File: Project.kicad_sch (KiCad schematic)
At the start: 60 parts, among them J1 Power terminal, J3 LED_pins, Q1 BC857, Q2 BC857, Q3 BC857, Q4 BC857, Q5 BC857, Q6 BC857, Q7 BC857, Q8 BC857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

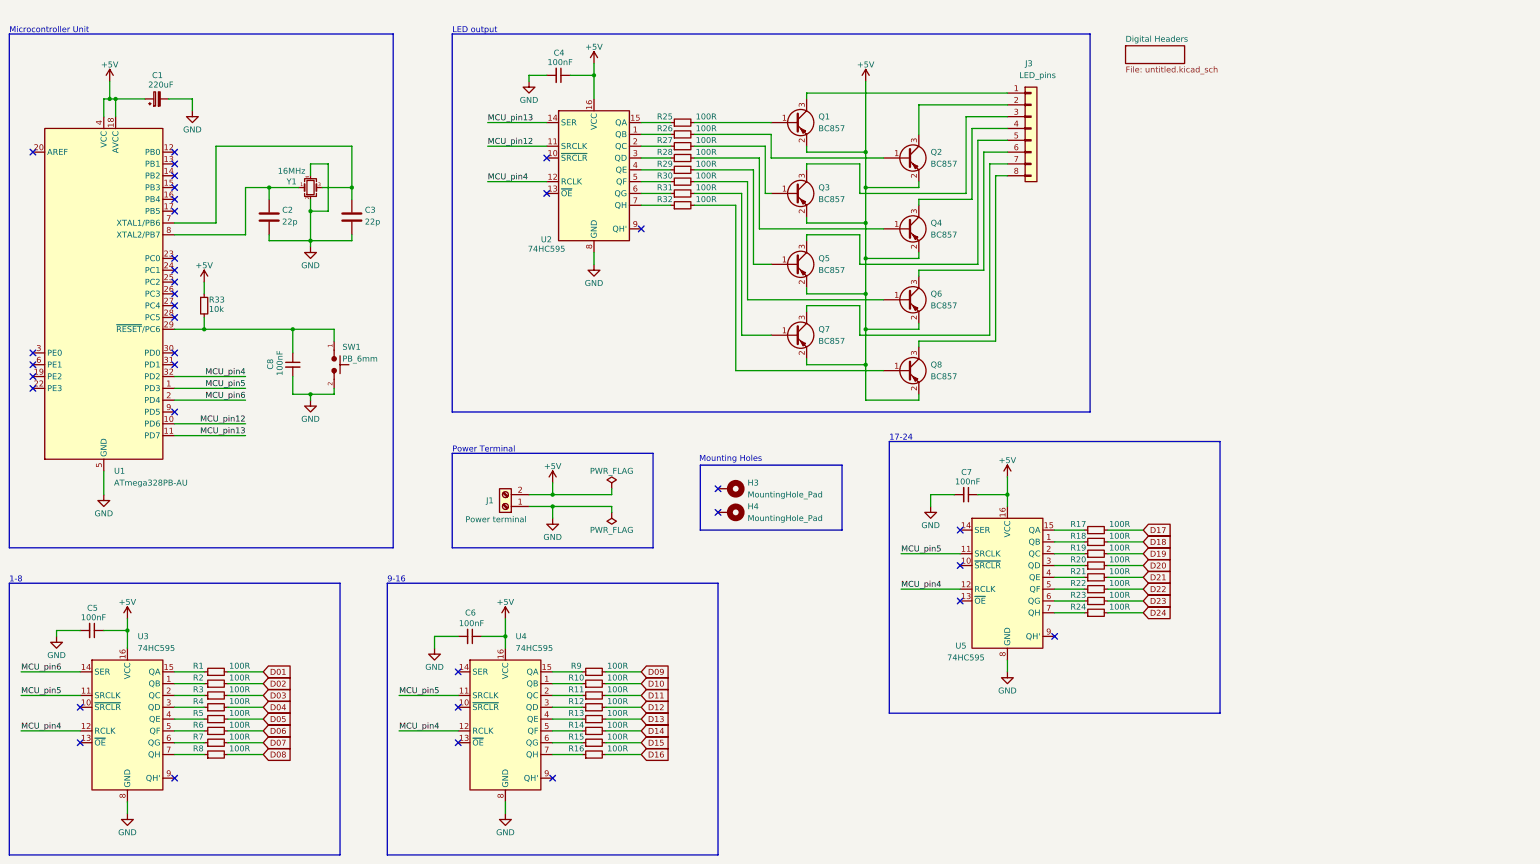
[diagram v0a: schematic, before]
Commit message: PCB design done, BOM still undecided
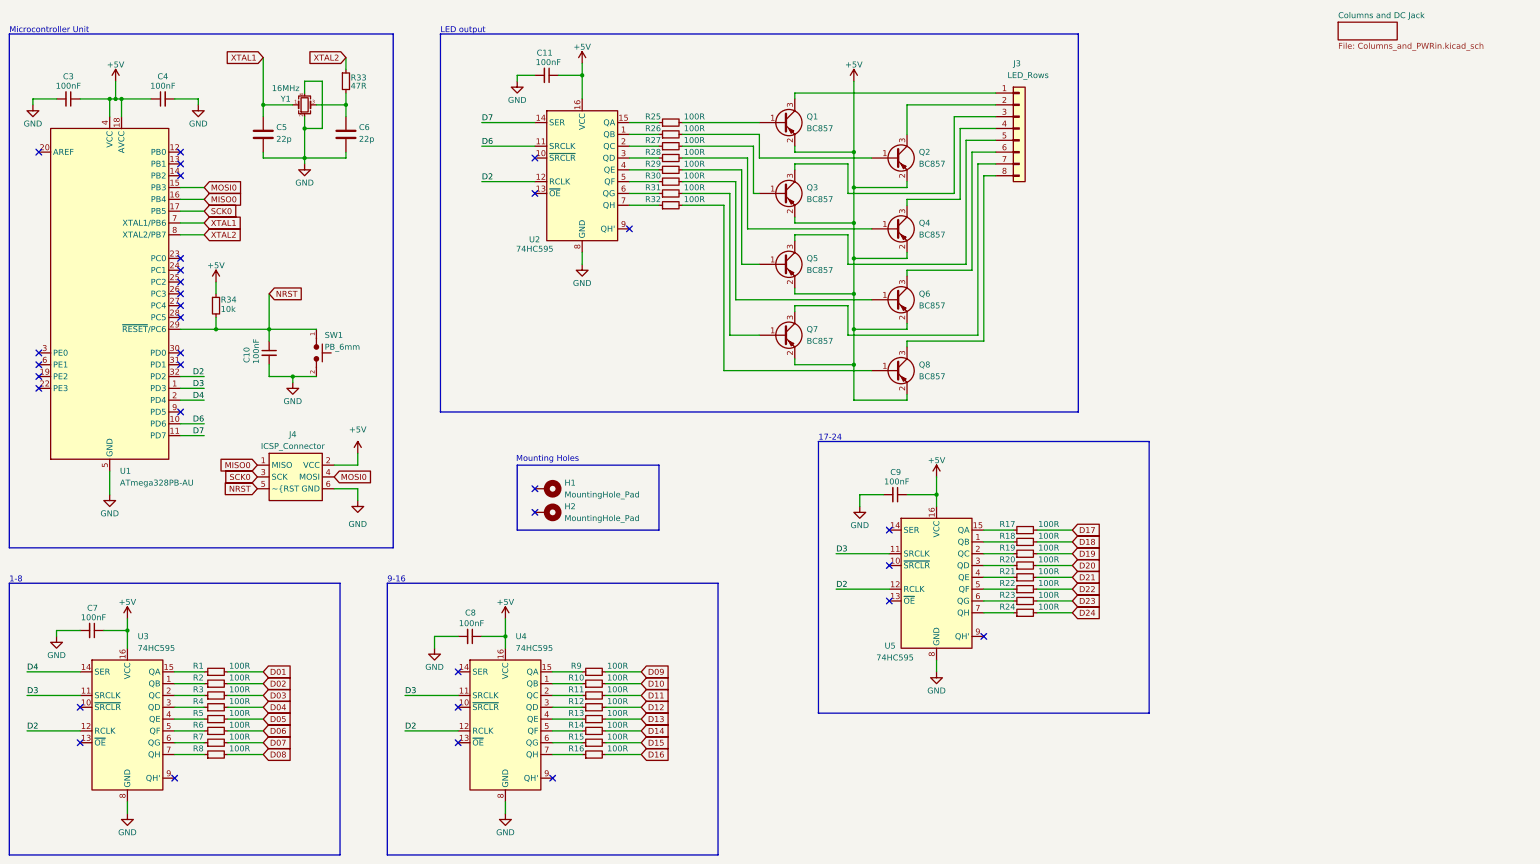
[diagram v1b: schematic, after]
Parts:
- removed C1: 220uF, Capacitor_SMD:CP_Elec_10x10, symbol Device:C_Polarized_Small
- removed C2, C3: 22p, Capacitor_SMD:C_0402_1005Metric, symbol Device:C
- removed H3, H4: MountingHole_Pad, MountingHole:MountingHole_3.2mm_M3_Pad_Via, symbol Mechanical:MountingHole_Pad
- removed J1: Power terminal, TerminalBlock_Phoenix:TerminalBlock_Phoenix_MKDS-1,5-2-5.08_1x02_P5.08mm_Horizontal, symbol Connector:Screw_Terminal_01x02
- added C3, C4: 100nF, Capacitor_SMD:C_0603_1608Metric, symbol Device:C_Small
- added C5, C6: 22p, Capacitor_SMD:C_0402_1005Metric, symbol Device:C
- added H1, H2: MountingHole_Pad, MountingHole:MountingHole_3.2mm_M3_Pad_Via, symbol Mechanical:MountingHole_Pad
- added J4: ICSP_Connector, Connector_PinHeader_2.54mm:PinHeader_2x03_P2.54mm_Vertical, symbol PCM_SL_Connectors:ICSP_Connector
- added R33: 47R, Resistor_SMD:R_0603_1608Metric, symbol Device:R_Small
- J3: value LED_pins -> LED_Rows
- renumbered C8 to C10, C4 to C11, C5 to C7, C6 to C8, C7 to C9, R33 to R34
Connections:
- net +5V: now also C3.1, C4.1, J4.2 (VCC)
- net GND: now also C3.2, C4.2, C5.2, C6.2, J4.6 (GND)
- net XTAL1: now reaches Y1.1
- net XTAL1: now also U1.7 (XTAL1/PB6), C5.1; no longer U1.8 (XTAL2/PB7)
- net at Y1.3: now also C6.1, R33.2; no longer U1.7 (XTAL1/PB6)
- net NRST: now reaches C10.1, R34.2, SW1.1, U1.29 (~{RESET}/PC6)
- net NRST: now also J4.5 (~{RST)
- net MOSI0: now reaches U1.15 (PB3)
- net MOSI0: now also J4.4 (MOSI)
- net MISO0: now reaches U1.16 (PB4)
- net MISO0: now also J4.1 (MISO)
- net SCK0: now reaches U1.17 (PB5)
- net SCK0: now also J4.3 (SCK)
- net MCU_pin12 renamed D6
- net MCU_pin13 renamed D7
- net MCU_pin4 renamed D2
- net MCU_pin5 renamed D3
- net MCU_pin6 renamed D4
- new net XTAL2: R33.1, U1.8 (XTAL2/PB7)
- no-connect marks 36 -> 33
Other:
- sheet Digital Headers renamed Columns and DC Jack
- sheet Columns and DC Jack: file untitled.kicad_sch -> Columns_and_PWRin.kicad_sch
- note removed: "Power Terminal"
- title: LED Array/ Digital Shifting with Atmega328 -> LED Array with Atmega328PB
- moved on the sheet: C10, C11, C9, J3, Q1, Q2, Q3, Q4, Q5, Q6, Q7, Q8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

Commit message: 595 column chip not daisy chained and  floating OE pins mistakes corrected
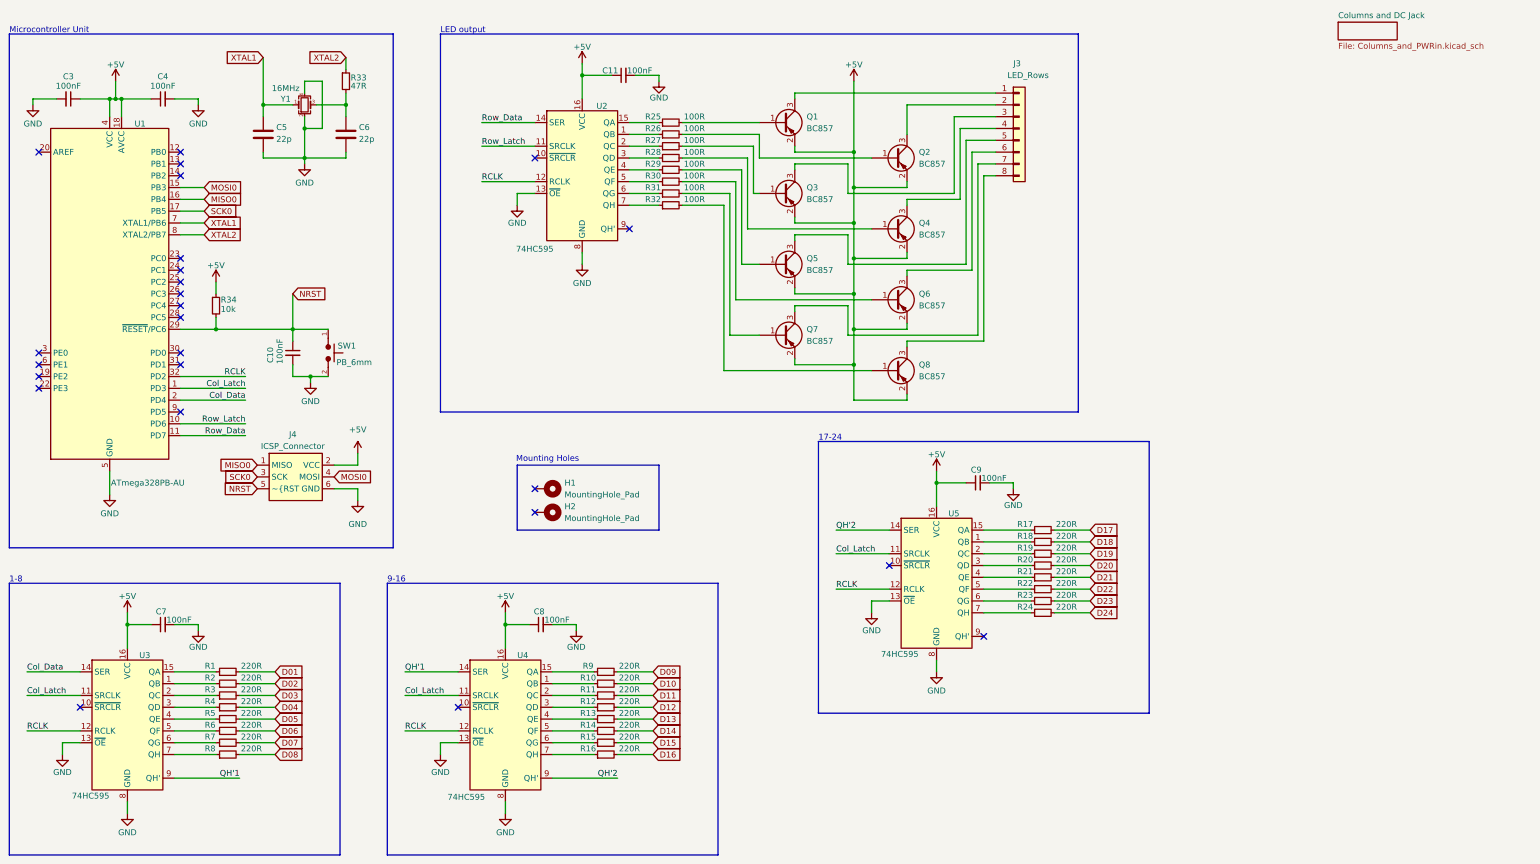
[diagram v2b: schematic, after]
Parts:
- R1, R10, R11, R12, R13, R14, R15, R16, R17, R18, R19, R2, R20, R21, R22, R23, R24, R3, R4, R5, R6, R7, R8, R9: value 100R -> 220R
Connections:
- net GND: now also U2.13 (~{OE}), U3.13 (~{OE}), U4.13 (~{OE}), U5.13 (~{OE})
- net QH'1: now reaches U4.14 (SER)
- net QH'1: now also U3.9 (QH')
- net QH'2: now reaches U4.9 (QH')
- net QH'2: now also U5.14 (SER)
- net D2 renamed RCLK
- net D3 renamed Col_Latch
- net D4 renamed Col_Data
- net D6 renamed Row_Latch
- net D7 renamed Row_Data
- no-connect marks 33 -> 25
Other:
- moved on the sheet: C10, C11, C7, C8, C9, R1, R10, R11, R12, R13, R14, R15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
